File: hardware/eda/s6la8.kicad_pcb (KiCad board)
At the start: 4 copper layers, 100 x 64 mm, 155 parts, among them J1 2.54mm 6 x 1 THT Vertical Male, J2 2.54mm 2 x 1 THT Vertical Male, J3 2.54mm 10 x 2 THT Horizontal 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, J4 USB4105-GF-A, J5 2.54mm 3 x 1 THT Vertical Male, U1 24LC128-I/SN, U10 XC6SLX9-2TQG144C, U11 CY7C68013A-56PVXC, U12 TLV62569DBVR, U13 TLV62569DBVR, U14 MT48LC16M16A2P-6A, U2 USBLC6-2SC6, U3 USBLC6-2SC6, U4 USBLC6-2SC6, U5 USBLC6-2SC6, U6 USBLC6-2SC6, U7 SN74LVC245APWR, U8 SN74LVC8T245PWR, U9 SN74LVC2T45DCUR, Y1 ASE-50.000MHZ-LC-T, Y2 24MHz 12pF

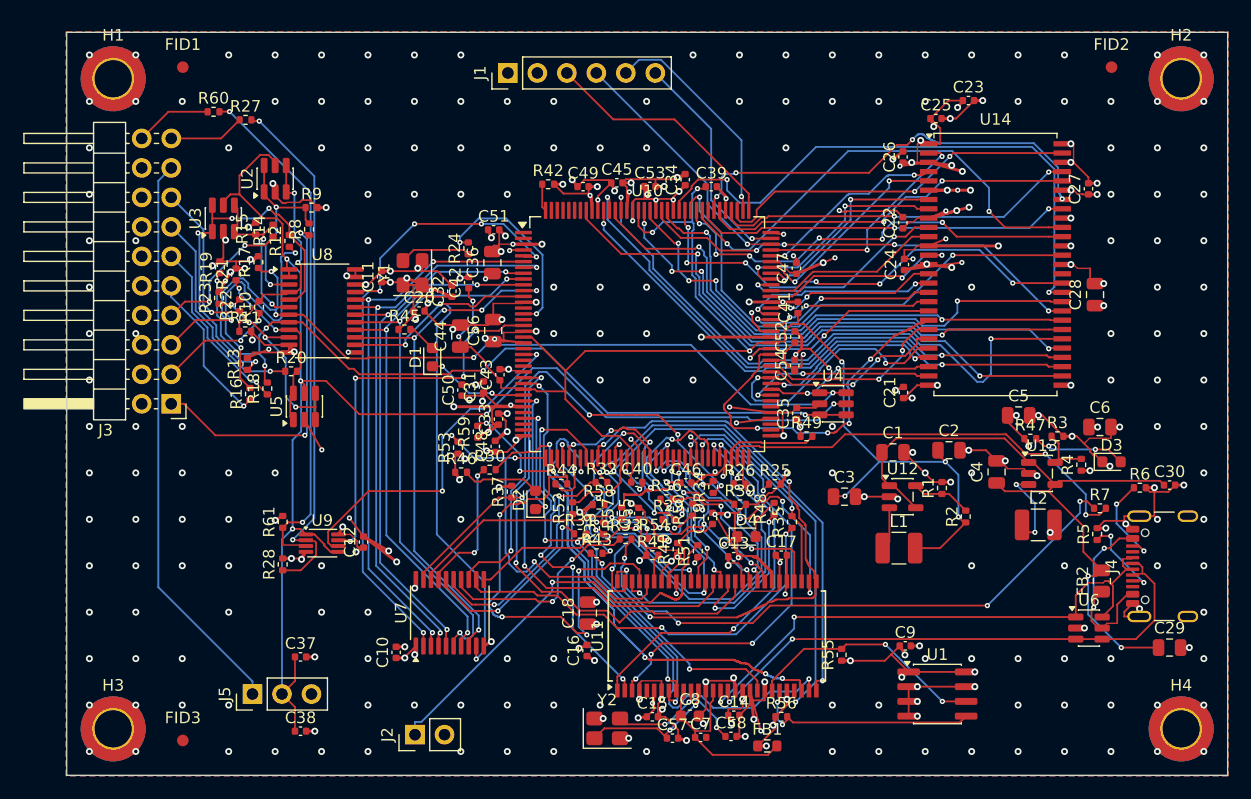
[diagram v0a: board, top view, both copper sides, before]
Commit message: Coupled 90-ohm USB pair, production silkscreen, firmware and driver side of board authentication, ISE container
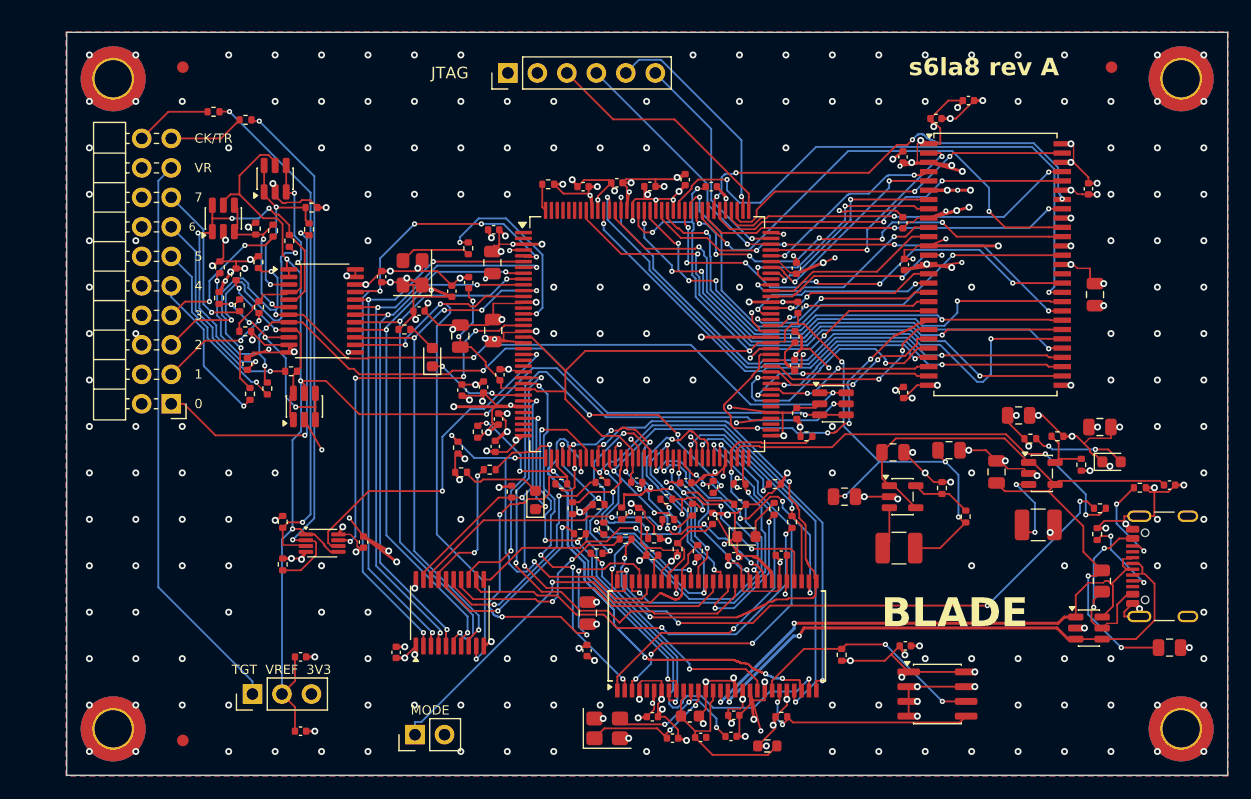
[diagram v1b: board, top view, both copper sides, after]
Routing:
- net USB_D_N: track 47.6 -> 48.8 mm
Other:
- board text added: "0"
- board text added: "1"
- board text added: "2"
- board text added: "3"
- board text added: "4"
- board text added: "5"
- board text added: "6"
- board text added: "7"
- board text added: "BLADE"
- board text added: "CK/TR"
- board text added: "JTAG"
- board text added: "MODE"
- board text added: "TGT VREF 3V3"
- board text added: "VR"
- board text added: "s6la8 rev A"
